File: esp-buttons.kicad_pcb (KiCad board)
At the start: 2 copper layers, 0 parts

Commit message: Initial placement of components on the PCB and PCB settings. Fixed the 3D model for the ESP-07
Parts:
- added C1: 4700uF, Capacitors_ThroughHole:C_Radial_D16_L25_P7.5, F.Cu at (83.8, 101.6)
- added C2: 100nF, Capacitors_SMD:C_1206_HandSoldering, F.Cu at (90.9, 83.1)
- added C3: 10uF, Capacitors_SMD:C_1210_HandSoldering, F.Cu at (111.3, 88.9)
- added C4: 10uF, Capacitors_SMD:C_1210_HandSoldering, F.Cu at (130.0, 132.8)
- added C5: 100nF, Capacitors_SMD:C_1206_HandSoldering, F.Cu at (130.3, 128.5)
- added C6: 10uF, Capacitors_SMD:C_1210_HandSoldering, F.Cu at (101.3, 124.7)
- added C7: 100nF, Capacitors_SMD:C_1206_HandSoldering, F.Cu at (96.5, 124.7)
- added C8: 100nF, Capacitors_SMD:C_1206_HandSoldering, F.Cu at (84.1, 124.7)
- added CON1: POWER_5V, Connect:JACK_ALIM, F.Cu at (68.6, 91.4)
- added D1: POWER_LED, LEDs:LED_1206, F.Cu at (113.0, 81.3)
- added D2: STATUS_LED, LEDs:LED_1206, F.Cu at (144.5, 104.6)
- added MT1: 1pin, Connect:1pin, F.Cu at (64.5, 75.4)
- added P1: CONN_BUTTON1, Terminal_Blocks:TerminalBlock_Pheonix_PT-3.5mm_4pol, F.Cu at (117.1, 145.2)
- added P2: CONN_BUTTON2, Terminal_Blocks:TerminalBlock_Pheonix_PT-3.5mm_4pol, F.Cu at (141.6, 145.4)
- added P3: CONN_BUTTON3, Terminal_Blocks:TerminalBlock_Pheonix_PT-3.5mm_4pol, F.Cu at (164.3, 145.2)
- added P4: CONN_BUTTON4, Terminal_Blocks:TerminalBlock_Pheonix_PT-3.5mm_4pol, F.Cu at (148.5, 80.4)
- added P5: CONN_BUTTON5, Terminal_Blocks:TerminalBlock_Pheonix_PT-3.5mm_4pol, F.Cu at (173.6, 80.5)
- added P6: UART_DEBUG, Pin_Headers:Pin_Header_Straight_1x02, F.Cu at (166.1, 129.5)
- added P7: UART, Pin_Headers:Pin_Header_Straight_1x04, F.Cu at (109.5, 121.7)
- added P8: POWER_5V, Terminal_Blocks:TerminalBlock_Pheonix_PT-3.5mm_2pol, F.Cu at (66.0, 104.1)
- added P9: USB, Connect:USB_B, F.Cu at (76.2, 129.5)
- added Q1: IRLML2502TRPBF, TO_SOT_Packages_SMD:SOT-23, F.Cu at (116.6, 137.2)
- added Q2: IRLML2502TRPBF, TO_SOT_Packages_SMD:SOT-23, F.Cu at (151.6, 138.7)
- added Q3: IRLML2502TRPBF, TO_SOT_Packages_SMD:SOT-23, F.Cu at (174.2, 137.9)
- added Q4: IRLML2502TRPBF, TO_SOT_Packages_SMD:SOT-23, F.Cu at (133.3, 88.9)
- added Q5: IRLML2502TRPBF, TO_SOT_Packages_SMD:SOT-23, F.Cu at (161.8, 87.9)
- added R1: 10K, Resistors_SMD:R_1206_HandSoldering, F.Cu at (127.3, 139.4)
- added R10: 10K, Resistors_SMD:R_1206_HandSoldering, F.Cu at (166.6, 93.2)
- added R11: 270, Resistors_SMD:R_1206_HandSoldering, F.Cu at (152.9, 104.9)
- added R2: 10K, Resistors_SMD:R_1206_HandSoldering, F.Cu at (144.0, 138.2)
- added R3: 10K, Resistors_SMD:R_1206_HandSoldering, F.Cu at (167.1, 137.4)
- added R4: 10K, Resistors_SMD:R_1206_HandSoldering, F.Cu at (141.7, 88.9)
- added R5: 10K, Resistors_SMD:R_1206_HandSoldering, F.Cu at (170.9, 87.4)
- added R6: 270, Resistors_SMD:R_1206_HandSoldering, F.Cu at (121.2, 81.0)
- added R7: 10K, Resistors_SMD:R_1206_HandSoldering, F.Cu at (136.9, 111.8)
- added R8: 10K, Resistors_SMD:R_1206_HandSoldering, F.Cu at (146.3, 113.3)
- added R9: 10K, Resistors_SMD:R_1206_HandSoldering, F.Cu at (148.3, 124.2)
- added SW1: RESET_BUTTON, Buttons_Switches_ThroughHole:SW_PUSH_6mm, F.Cu at (141.5, 122.2)
- added SW2: PROG_BUTTON, Buttons_Switches_ThroughHole:SW_PUSH_6mm, F.Cu at (148.1, 94.5)
- added U1: ESP-07v2, ESP8266:ESP-07v2, F.Cu at (176.5, 108.7)
- added U2: LD1117S33CTR, TO_SOT_Packages_SMD:TO-263-3Lead, F.Cu at (100.3, 92.7)
- added U3: FT230XS, Housings_SSOP:SSOP-16_3.9x4.9mm_Pitch0.635mm, F.Cu at (90.2, 124.5)
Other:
- board outline added: 118.1 x 81.3 mm
- net class Default: clearance 0.2 -> 0.254; trace_width 0.25 -> 0.254
- rule trace_clearance: 0.2 -> 0.254
- rule trace_min: 0.2 -> 0.254

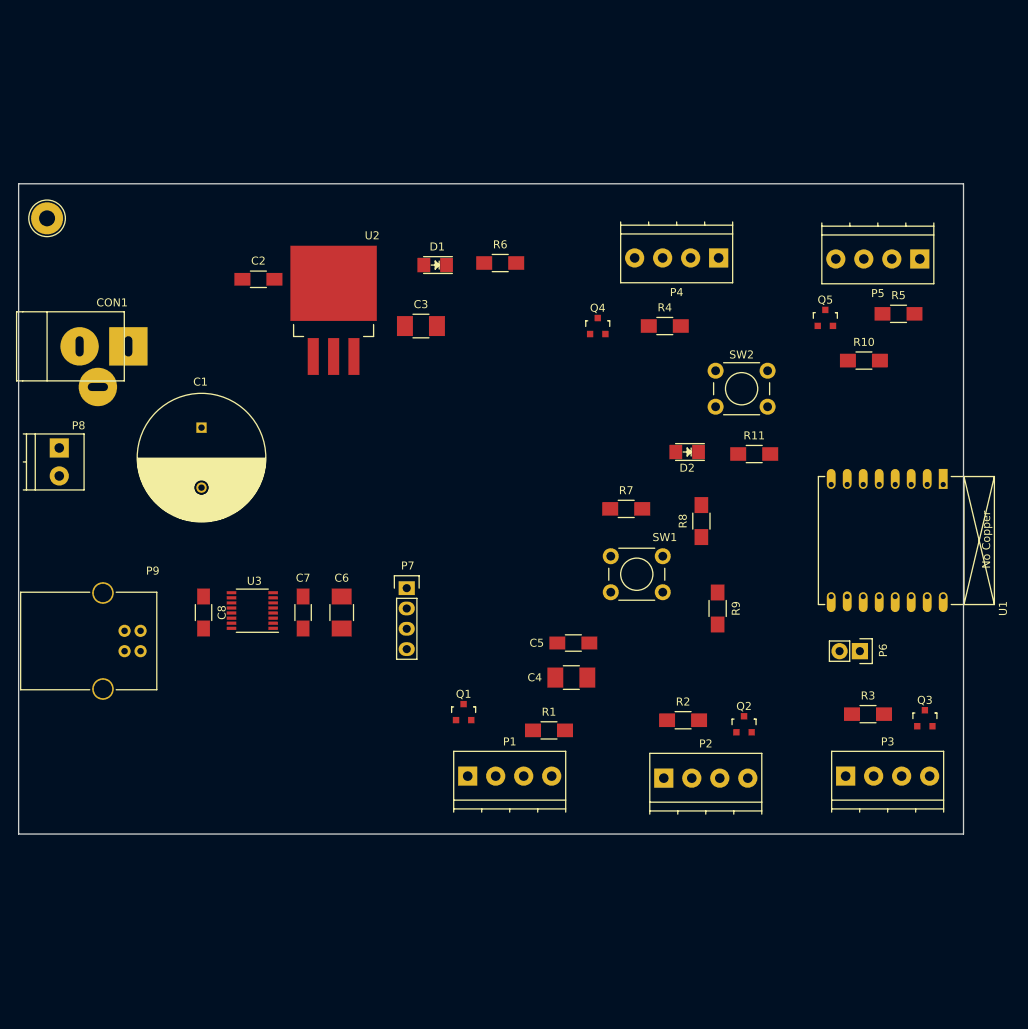
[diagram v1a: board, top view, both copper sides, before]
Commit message: Added the 3 remaining mounting holes
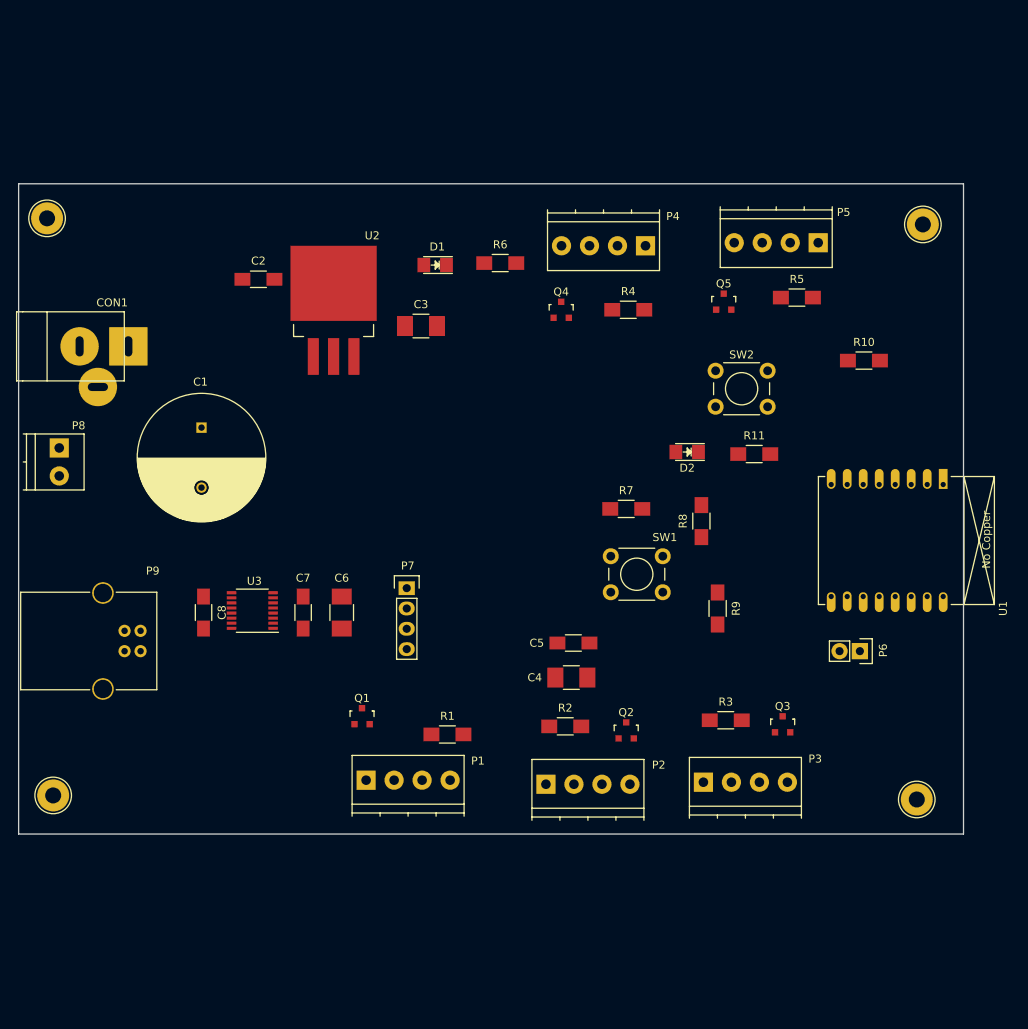
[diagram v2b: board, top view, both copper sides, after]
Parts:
- added MT2: 1pin, Connect:1pin, F.Cu at (65.3, 147.6)
- added MT3: 1pin, Connect:1pin, F.Cu at (173.2, 148.1)
- added MT4: 1pin, Connect:1pin, F.Cu at (174.0, 76.2)
- moved P3 17.8 mm to (146.6, 145.9)
- moved Q3 17.8 mm to (156.5, 138.7)
- moved R3 17.8 mm to (149.4, 138.2)
- moved Q2 14.8 mm to (136.9, 139.4)
- moved R2 14.8 mm to (129.3, 138.9)
- moved P2 14.8 mm to (126.9, 146.2)
- moved R5 12.9 mm to (158.2, 85.3)
- moved P5 12.9 mm to (160.9, 78.5)
- moved Q5 12.9 mm to (149.1, 85.9)
- moved Q1 12.7 mm to (103.9, 137.7)
- moved R1 12.7 mm to (114.6, 140.0)
- moved P1 12.7 mm to (104.4, 145.7)
- moved P4 9.27 mm to (139.3, 78.9)
- moved Q4 5.00 mm to (128.8, 86.9)
- moved R4 5.00 mm to (137.2, 86.9)
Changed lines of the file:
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@@
     (tracks 0)
     (zones 0)
-    (modules 42)
+    (modules 45)
     (nets 35)
   )
@@
     (add_net "Net-(U3-Pad6)")
     (add_net "Net-(U3-Pad7)")
+  )
+  (module Connect:1pin (layer F.Cu)
+    (at 173.99 76.2)
+    (descr "module 1 pin (ou trou mecanique de percage)")
+    (tags DEV)
+    (fp_text reference MT4 (at 0 -3.048) (layer F.SilkS) hide
+      (effects (font (size 1 1) (thickness 0.15)))
+    )
+    (fp_text value 1pin (at 0 2.794) (layer F.Fab) hide
+      (effects (font (size 1 1) (thickness 0.15)))
+    )
+    (fp_circle (center 0 0) (end 0 -2.286) (layer F.SilkS) (width 0.15))
+    (pad 1 thru_hole circle (at 0 0) (size 4 4) (drill 2) (layers *.Cu *.Mask F.SilkS))
+  )
+  (module Connect:1pin (layer F.Cu)
+    (at 173.228 148.082)
+    (descr "module 1 pin (ou trou mecanique de percage)")
+    (tags DEV)
+    (fp_text reference MT3 (at 0 -3.048) (layer F.SilkS) hide
+      (effects (font (size 1 1) (thickness 0.15)))
+    )
+    (fp_text value 1pin (at 0 2.794) (layer F.Fab) hide
+      (effects (font (size 1 1) (thickness 0.15)))
+    )
+    (fp_circle (center 0 0) (end 0 -2.286) (layer F.SilkS) (width 0.15))
+    (pad 1 thru_hole circle (at 0 0) (size 4 4) (drill 2) (layers *.Cu *.Mask F.SilkS))
+  )
+  (module Connect:1pin (layer F.Cu)
+    (at 65.278 147.574)
+    (descr "module 1 pin (ou trou mecanique de percage)")
+    (tags DEV)
+    (fp_text reference MT2 (at 0 -3.048) (layer F.SilkS) hide
+      (effects (font (size 1 1) (thickness 0.15)))
+    )
+    (fp_text value 1pin (at 0 2.794) (layer F.Fab) hide
+      (effects (font (size 1 1) (thickness 0.15)))
+    )
+    (fp_circle (center 0 0) (end 0 -2.286) (layer F.SilkS) (width 0.15))
+    (pad 1 thru_hole circle (at 0 0) (size 4 4) (drill 2) (layers *.Cu *.Mask F.SilkS))
   )
   (module Capacitors_ThroughHole:C_Radial_D16_L25_P7.5 (layer F.Cu)
@@
   )
   (module Terminal_Blocks:TerminalBlock_Pheonix_PT-3.5mm_4pol (layer F.Cu)
-    (at 117.094 145.161)
+    (at 104.394 145.669)
     (descr "4-way 3.5mm pitch terminal block, Phoenix PT series")
-    (fp_text reference P1 (at 5.25 -4.3) (layer F.SilkS)
+    (fp_text reference P1 (at 13.97 -2.413) (layer F.SilkS)
       (effects (font (size 1 1) (thickness 0.15)))
     )
@@
   )
   (module Terminal_Blocks:TerminalBlock_Pheonix_PT-3.5mm_4pol (layer F.Cu)
-    (at 164.338 145.161)
+    (at 146.558 145.923)
     (descr "4-way 3.5mm pitch terminal block, Phoenix PT series")
-    (fp_text reference P3 (at 5.25 -4.3) (layer F.SilkS)
+    (fp_text reference P3 (at 13.97 -2.921) (layer F.SilkS)
       (effects (font (size 1 1) (thickness 0.15)))
     )
@@
   )
   (module Terminal_Blocks:TerminalBlock_Pheonix_PT-3.5mm_4pol (layer F.Cu)
-    (at 148.463 80.391 180)
+    (at 139.319 78.867 180)
     (descr "4-way 3.5mm pitch terminal block, Phoenix PT series")
-    (fp_text reference P4 (at 5.25 -4.3 180) (layer F.SilkS)
+    (fp_text reference P4 (at -3.429 3.683 180) (layer F.SilkS)
       (effects (font (size 1 1) (thickness 0.15)))
     )
@@
   )
   (module Terminal_Blocks:TerminalBlock_Pheonix_PT-3.5mm_4pol (layer F.Cu)
-    (at 173.609 80.518 180)
+    (at 160.909 78.486 180)
     (descr "4-way 3.5mm pitch terminal block, Phoenix PT series")
-    (fp_text reference P5 (at 5.25 -4.3 180) (layer F.SilkS)
+    (fp_text reference P5 (at -3.175 3.81 180) (layer F.SilkS)
       (effects (font (size 1 1) (thickness 0.15)))
     )
@@
   )
   (module TO_SOT_Packages_SMD:SOT-23 (layer F.Cu)
-    (at 116.586 137.16)
+    (at 103.886 137.668)
     (descr "SOT-23, Standard")
     (tags SOT-23)
@@
   )
   (module TO_SOT_Packages_SMD:SOT-23 (layer F.Cu)
-    (at 151.638 138.684)
+    (at 136.906 139.446)
     (descr "SOT-23, Standard")
     (tags SOT-23)
@@
   )
   (module TO_SOT_Packages_SMD:SOT-23 (layer F.Cu)
-    (at 174.244 137.922)
+    (at 156.464 138.684)
     (descr "SOT-23, Standard")
     (tags SOT-23)
@@
   )
   (module TO_SOT_Packages_SMD:SOT-23 (layer F.Cu)
-    (at 133.35 88.9)
+    (at 128.778 86.868)
     (descr "SOT-23, Standard")
     (tags SOT-23)
@@
   )
   (module TO_SOT_Packages_SMD:SOT-23 (layer F.Cu)
-    (at 161.798 87.884)
+    (at 149.098 85.852)
     (descr "SOT-23, Standard")
     (tags SOT-23)
@@
   )
   (module Resistors_SMD:R_1206_HandSoldering (layer F.Cu)
-    (at 127.254 139.446)
+    (at 114.554 139.954)
     (descr "Resistor SMD 1206, hand soldering")
     (tags "resistor 1206")
@@
   )
   (module Resistors_SMD:R_1206_HandSoldering (layer F.Cu)
-    (at 144.018 138.176)
+    (at 129.286 138.938)
     (descr "Resistor SMD 1206, hand soldering")
     (tags "resistor 1206")
@@
   )
   (module Resistors_SMD:R_1206_HandSoldering (layer F.Cu)
-    (at 167.132 137.414)
+    (at 149.352 138.176)
     (descr "Resistor SMD 1206, hand soldering")
     (tags "resistor 1206")
@@
   )
   (module Resistors_SMD:R_1206_HandSoldering (layer F.Cu)
-    (at 141.732 88.9)
+    (at 137.16 86.868)
     (descr "Resistor SMD 1206, hand soldering")
     (tags "resistor 1206")
@@
   )
   (module Resistors_SMD:R_1206_HandSoldering (layer F.Cu)
-    (at 170.942 87.376)
+    (at 158.242 85.344)
     (descr "Resistor SMD 1206, hand soldering")
     (tags "resistor 1206")
@@
   )
   (module Terminal_Blocks:TerminalBlock_Pheonix_PT-3.5mm_4pol (layer F.Cu)
-    (at 141.605 145.415)
+    (at 126.873 146.177)
     (descr "4-way 3.5mm pitch terminal block, Phoenix PT series")
-    (fp_text reference P2 (at 5.25 -4.3) (layer F.SilkS)
-      (effects (font (size 1 1) (thickness 0.15)))
-    )
+    (fp_text reference P2 (at 14.097 -2.413) (layer F.SilkS)
+      (effects (font (size 1 1) (thickness 0.15)))
+    )

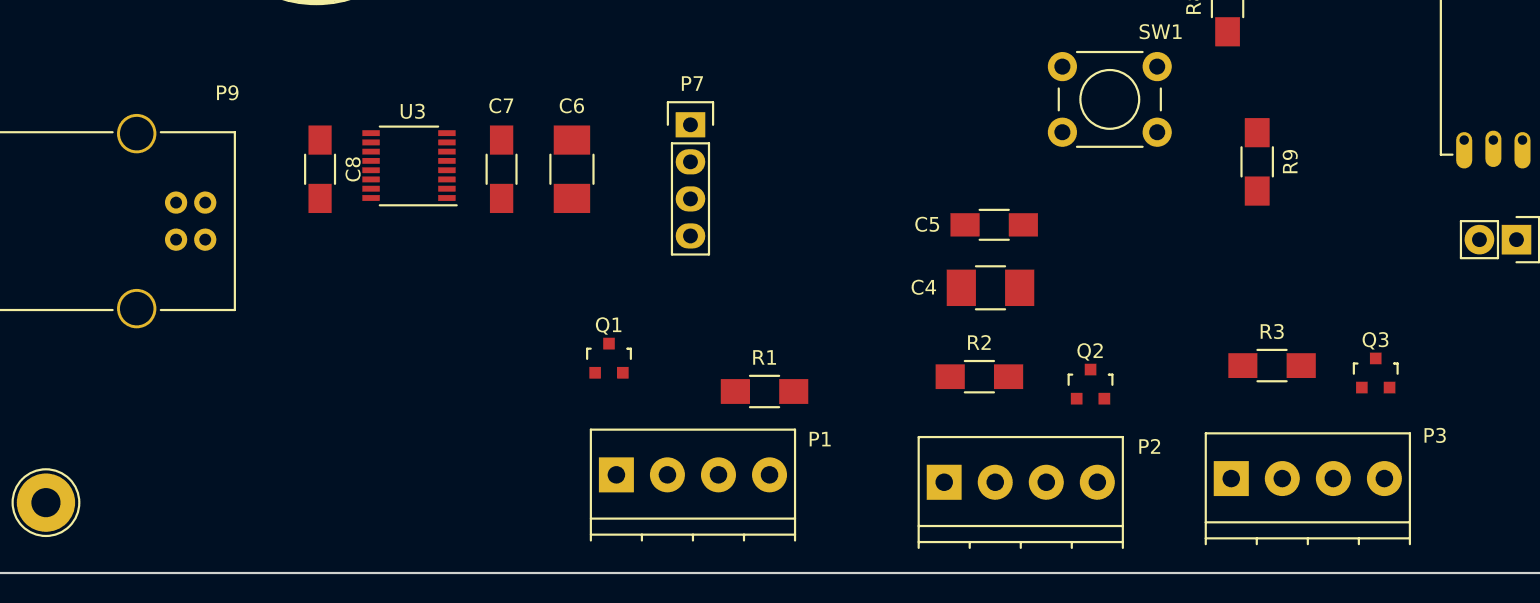
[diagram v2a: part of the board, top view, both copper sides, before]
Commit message: Added title text on top silkscreen
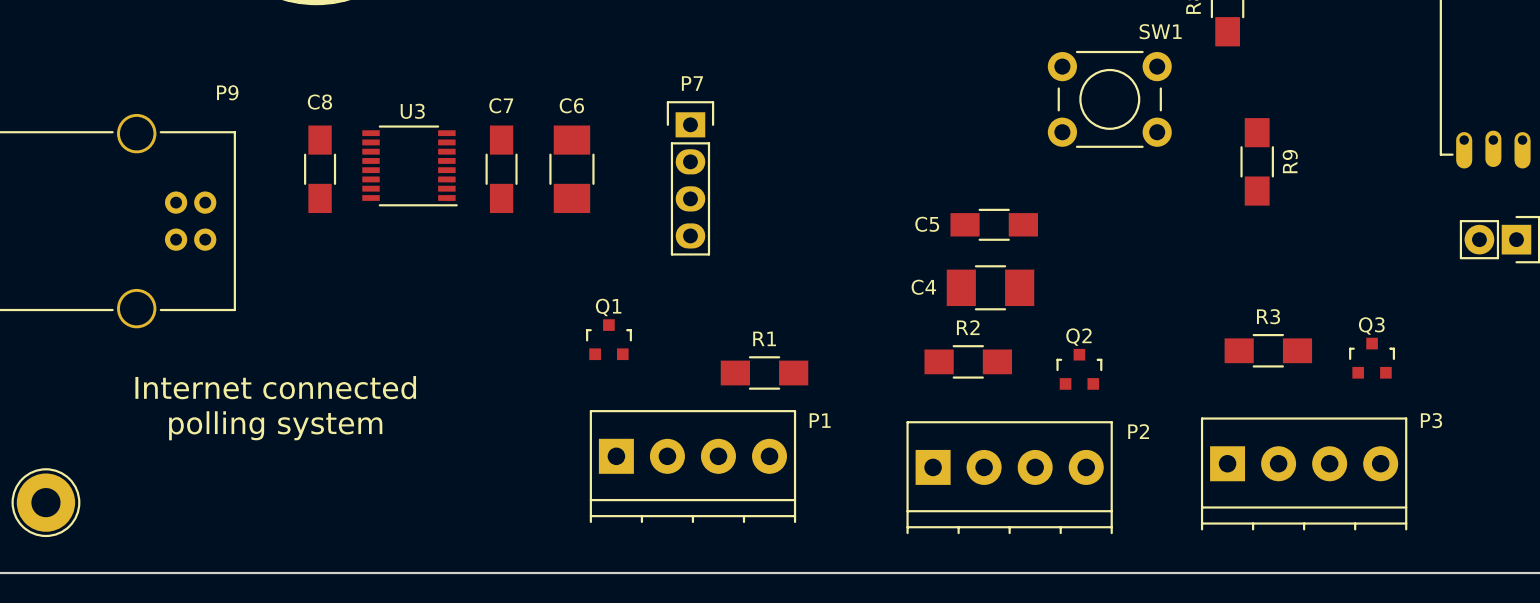
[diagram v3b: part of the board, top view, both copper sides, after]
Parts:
- moved P1 1.27 mm to (104.4, 144.4)
- moved Q1 1.27 mm to (103.9, 136.4)
- moved R1 1.27 mm to (114.6, 138.7)
- moved P2 1.27 mm to (126.1, 145.2)
- moved Q2 1.27 mm to (136.1, 138.4)
- moved R2 1.27 mm to (128.5, 137.9)
- moved P3 1.05 mm to (146.3, 144.9)
- moved Q3 1.05 mm to (156.2, 137.7)
- moved R3 1.05 mm to (149.1, 137.2)
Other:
- board text added: "Internet connected polling system"
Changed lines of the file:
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@@
     (area 60.884999 71.044999 179.145001 152.475001)
     (thickness 1.6)
-    (drawings 4)
+    (drawings 5)
     (tracks 0)
     (zones 0)
@@
     (tags "capacitor 1206")
     (attr smd)
-    (fp_text reference C8 (at 0 -2.3 270) (layer F.SilkS)
+    (fp_text reference C8 (at -4.572 0 360) (layer F.SilkS)
       (effects (font (size 1 1) (thickness 0.15)))
     )
@@
   )
   (module Terminal_Blocks:TerminalBlock_Pheonix_PT-3.5mm_4pol (layer F.Cu)
-    (at 104.394 145.669)
+    (at 104.394 144.399)
     (descr "4-way 3.5mm pitch terminal block, Phoenix PT series")
     (fp_text reference P1 (at 13.97 -2.413) (layer F.SilkS)
@@
   )
   (module Terminal_Blocks:TerminalBlock_Pheonix_PT-3.5mm_4pol (layer F.Cu)
-    (at 146.558 145.923)
+    (at 146.304 144.907)
     (descr "4-way 3.5mm pitch terminal block, Phoenix PT series")
     (fp_text reference P3 (at 13.97 -2.921) (layer F.SilkS)
@@
       (effects (font (size 1 1) (thickness 0.15)))
     )
-    (fp_text value USB (at -0.254 -7.493 360) (layer F.Fab)
+    (fp_text value USB (at -0.254 -7.493 180) (layer F.Fab)
       (effects (font (size 1 1) (thickness 0.15)))
     )
@@
   )
   (module TO_SOT_Packages_SMD:SOT-23 (layer F.Cu)
-    (at 103.886 137.668)
+    (at 103.886 136.398)
     (descr "SOT-23, Standard")
     (tags SOT-23)
@@
   )
   (module TO_SOT_Packages_SMD:SOT-23 (layer F.Cu)
-    (at 136.906 139.446)
+    (at 136.144 138.43)
     (descr "SOT-23, Standard")
     (tags SOT-23)
@@
   )
   (module TO_SOT_Packages_SMD:SOT-23 (layer F.Cu)
-    (at 156.464 138.684)
+    (at 156.21 137.668)
     (descr "SOT-23, Standard")
     (tags SOT-23)
@@
   )
   (module Resistors_SMD:R_1206_HandSoldering (layer F.Cu)
-    (at 114.554 139.954)
+    (at 114.554 138.684)
     (descr "Resistor SMD 1206, hand soldering")
     (tags "resistor 1206")
@@
   )
   (module Resistors_SMD:R_1206_HandSoldering (layer F.Cu)
-    (at 129.286 138.938)
+    (at 128.524 137.922)
     (descr "Resistor SMD 1206, hand soldering")
     (tags "resistor 1206")
@@
   )
   (module Resistors_SMD:R_1206_HandSoldering (layer F.Cu)
-    (at 149.352 138.176)
+    (at 149.098 137.16)
     (descr "Resistor SMD 1206, hand soldering")
     (tags "resistor 1206")
@@
   )
   (module Terminal_Blocks:TerminalBlock_Pheonix_PT-3.5mm_4pol (layer F.Cu)
-    (at 126.873 146.177)
+    (at 126.111 145.161)
     (descr "4-way 3.5mm pitch terminal block, Phoenix PT series")
     (fp_text reference P2 (at 14.097 -2.413) (layer F.SilkS)
@@
     (pad 1 thru_hole circle (at 0 0) (size 4 4) (drill 2) (layers *.Cu *.Mask F.SilkS))
   )
+  (gr_text "Internet connected\npolling system" (at 81.026 140.97) (layer F.SilkS)
+    (effects (font (size 1.5 1.5) (thickness 0.3)))
+  )
   (gr_line (start 179.07 152.4) (end 60.96 152.4) (angle 90) (layer Edge.Cuts) (width 0.15))
